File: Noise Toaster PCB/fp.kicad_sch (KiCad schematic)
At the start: 29 parts, among them J1 Line Out, SW1 Manual Gate, SW2 Repeat

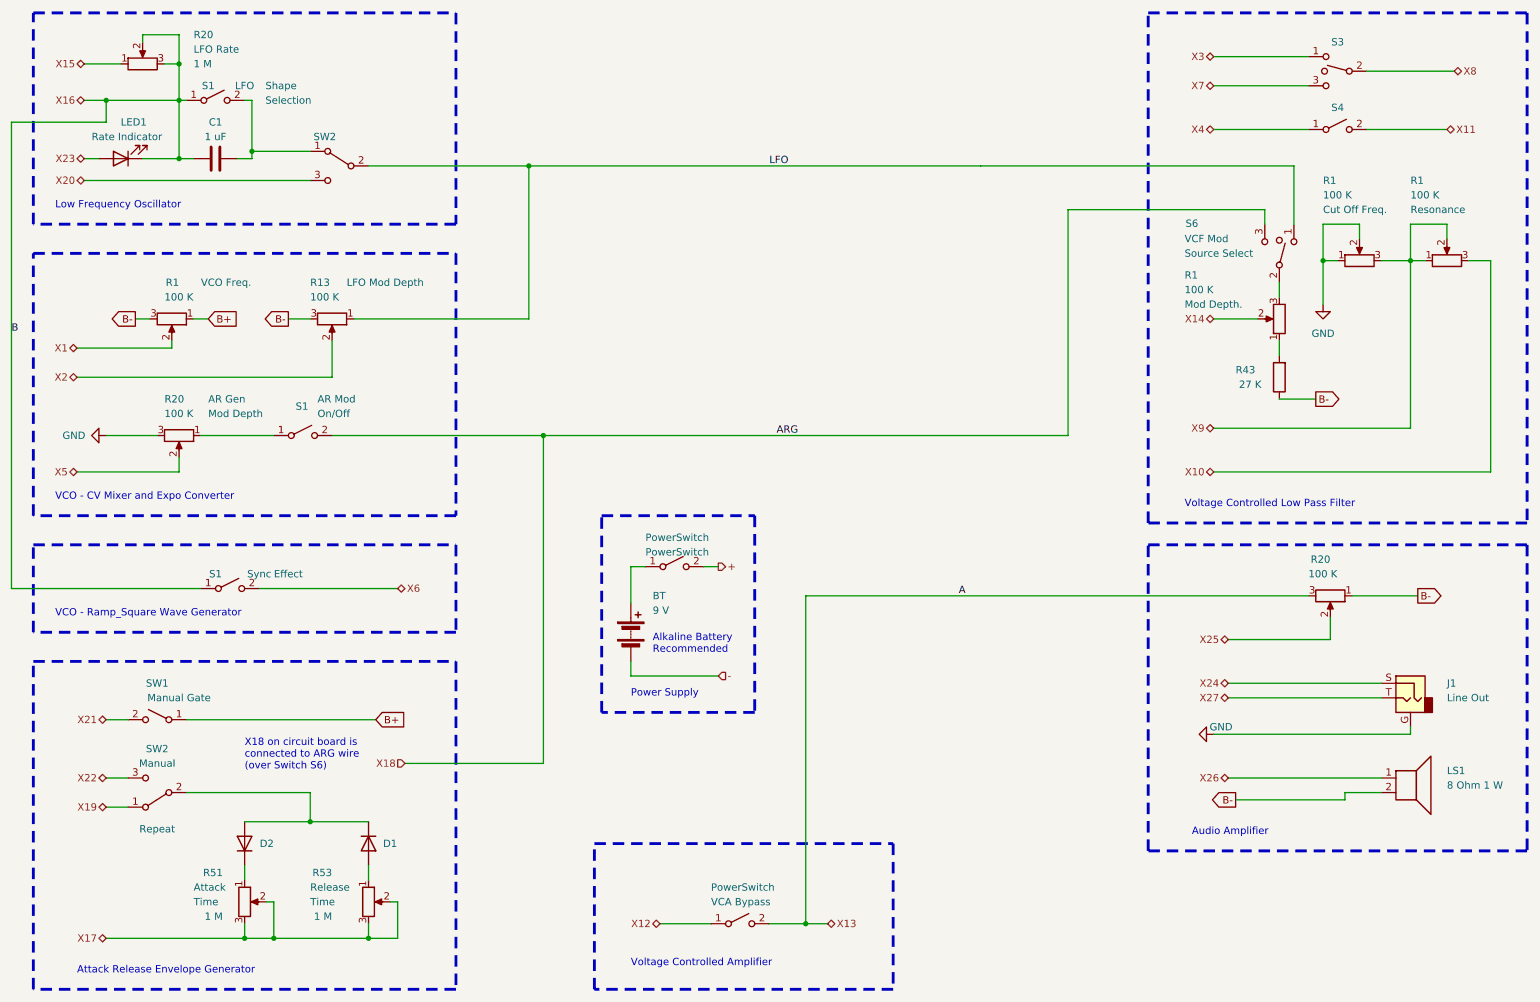
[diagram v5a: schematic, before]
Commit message: added front panel pcb
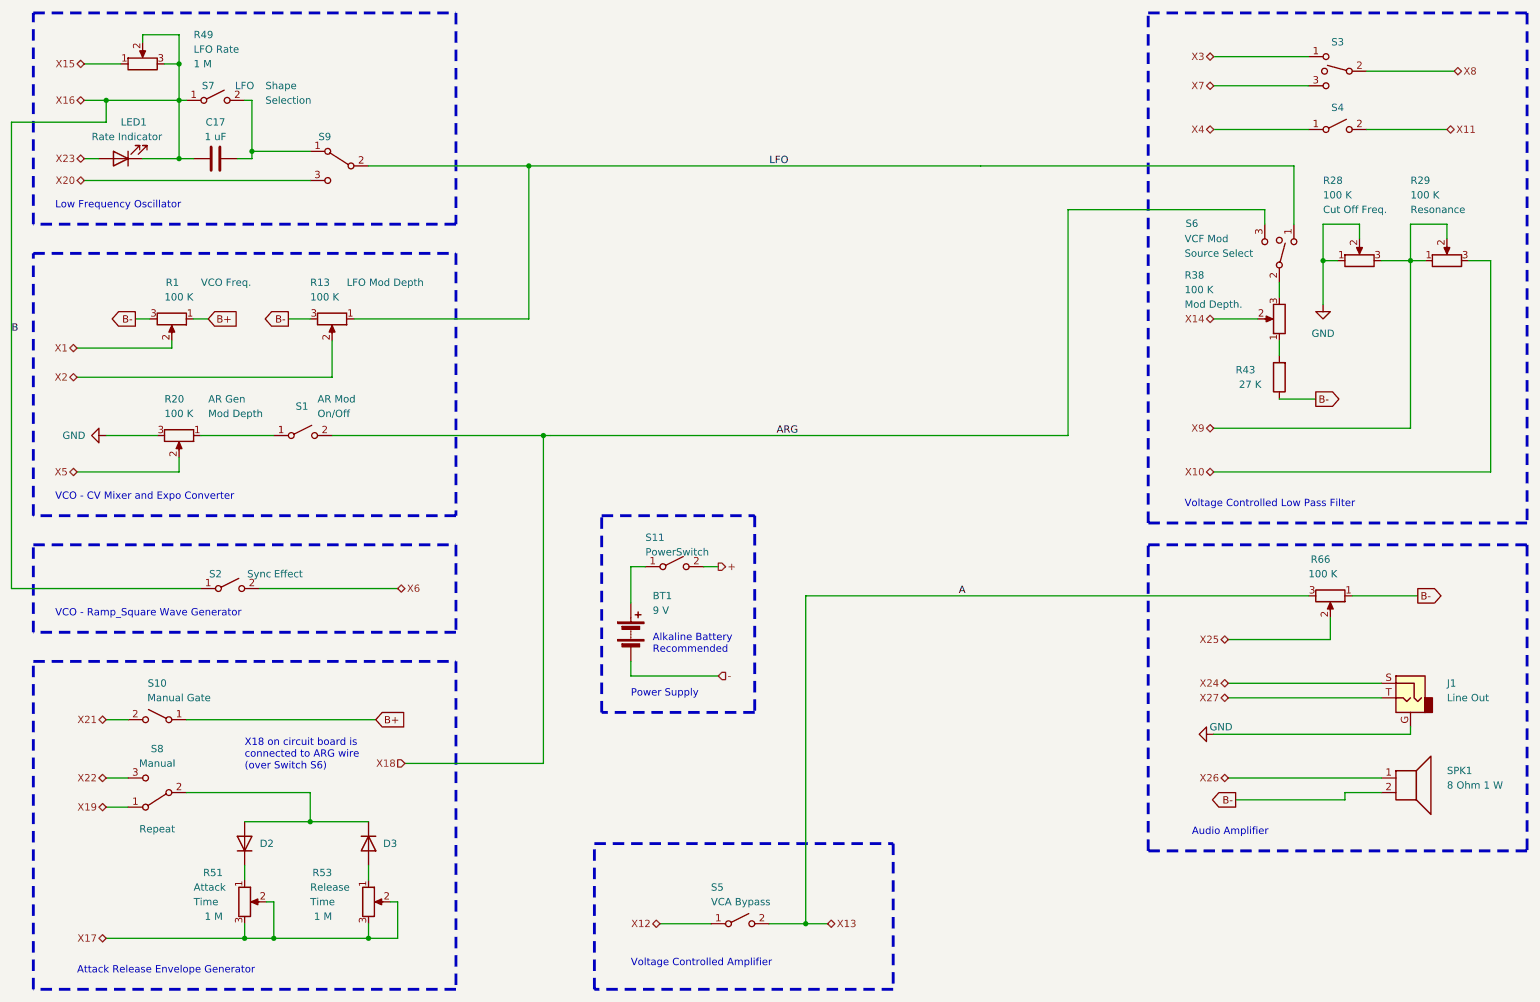
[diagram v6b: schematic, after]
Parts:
- renumbered BT to BT1, C1 to C17, D1 to D3, R1 to R28, R1 to R29, R1 to R38, R20 to R49, R20 to R66, SW1 to S10, PowerSwitch to S11, S1 to S2, PowerSwitch to S5, S1 to S7, SW2 to S8, SW2 to S9, LS1 to SPK1
